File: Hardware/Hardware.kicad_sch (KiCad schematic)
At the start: 0 parts

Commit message: Finished SCH MCU
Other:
- added sheet IMU (IMU.kicad_sch)
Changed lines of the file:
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@@
 	(paper "A4")
 	(sheet
-		(at 166.37 92.71)
-		(size 73.66 48.26)
+		(at 59.69 35.56)
+		(size 36.83 19.05)
+		(fields_autoplaced yes)
+		(stroke
+			(width 0.1524)
+			(type solid)
+		)
+		(fill
+			(color 0 0 0 0.0000)
+		)
+		(property "Sheetname" "IMU"
+			(at 59.69 34.8484 0)
+			(effects
+				(font
+					(size 1.27 1.27)
+				)
+				(justify left bottom)
+			)
+		)
+		(property "Sheetfile" "IMU.kicad_sch"
+			(at 59.69 55.1946 0)
+			(effects
+				(font
+					(size 1.27 1.27)
+				)
+				(justify left top)
+			)
+		)
+		(instances
+			(project "Hardware"
+				(path "/8d39550c-1c23-48e1-ae23-c502e9088467"
+					(page "3")
+				)
+			)
+		)
+	)
+	(sheet
+		(at 15.24 17.78)
+		(size 21.59 48.26)
 		(fields_autoplaced yes)
 		(stroke
@@
 		)
 		(property "Sheetname" "MCU_Core"
-			(at 166.37 91.9984 0)
+			(at 15.24 17.0684 0)
 			(effects
 				(font
@@
 		)
 		(property "Sheetfile" "MCU_Core.kicad_sch"
-			(at 166.37 141.5546 0)
+			(at 15.24 66.6246 0)
 			(effects
 				(font

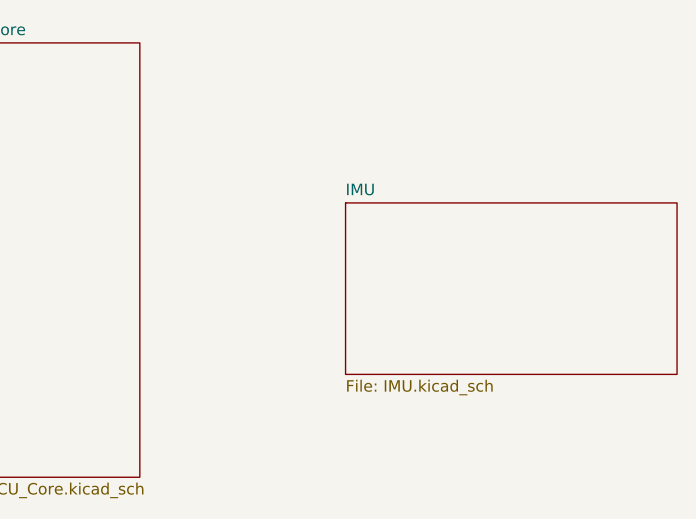
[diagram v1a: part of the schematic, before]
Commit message: Finished IMU SCH
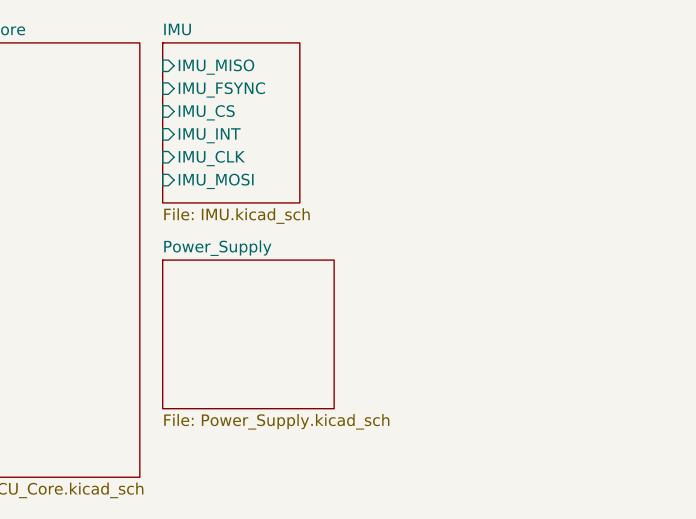
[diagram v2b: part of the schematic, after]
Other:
- added sheet Power_Supply (Power_Supply.kicad_sch)
- sheet IMU ports: added IMU_CLK, IMU_CS, IMU_FSYNC, IMU_INT, IMU_MISO, IMU_MOSI; removed none
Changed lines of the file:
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@@
 	(paper "A4")
 	(sheet
-		(at 59.69 35.56)
-		(size 36.83 19.05)
+		(at 39.37 17.78)
+		(size 15.24 17.78)
 		(fields_autoplaced yes)
 		(stroke
@@
 		)
 		(property "Sheetname" "IMU"
-			(at 59.69 34.8484 0)
+			(at 39.37 17.0684 0)
 			(effects
 				(font
@@
 		)
 		(property "Sheetfile" "IMU.kicad_sch"
-			(at 59.69 55.1946 0)
+			(at 39.37 36.1446 0)
 			(effects
 				(font
@@
 				)
 				(justify left top)
+			)
+		)
+		(pin "IMU_MISO" input
+			(at 39.37 20.32 180)
+			(effects
+				(font
+					(size 1.27 1.27)
+				)
+				(justify left)
+			)
+		)
+		(pin "IMU_FSYNC" input
+			(at 39.37 22.86 180)
+			(effects
+				(font
+					(size 1.27 1.27)
+				)
+				(justify left)
+			)
+		)
+		(pin "IMU_CS" input
+			(at 39.37 25.4 180)
+			(effects
+				(font
+					(size 1.27 1.27)
+				)
+				(justify left)
+			)
+		)
+		(pin "IMU_INT" input
+			(at 39.37 27.94 180)
+			(effects
+				(font
+					(size 1.27 1.27)
+				)
+				(justify left)
+			)
+		)
+		(pin "IMU_CLK" input
+			(at 39.37 30.48 180)
+			(effects
+				(font
+					(size 1.27 1.27)
+				)
+				(justify left)
+			)
+		)
+		(pin "IMU_MOSI" input
+			(at 39.37 33.02 180)
+			(effects
+				(font
+					(size 1.27 1.27)
+				)
+				(justify left)
 			)
 		)
@@
 				)
 			)
+		)
+	)
+	(sheet
+		(at 39.37 41.91)
+		(size 19.05 16.51)
+		(fields_autoplaced yes)
+		(stroke
+			(width 0.1524)
+			(type solid)
+		)
+		(fill
+			(color 0 0 0 0.0000)
+		)
+		(property "Sheetname" "Power_Supply"
+			(at 39.37 41.1984 0)
+			(effects
+				(font
+					(size 1.27 1.27)
+				)
+				(justify left bottom)
+			)
+		)
+		(property "Sheetfile" "Power_Supply.kicad_sch"
+			(at 39.37 59.0046 0)
+			(effects
+				(font
+					(size 1.27 1.27)
+				)
+				(justify left top)
+			)
+		)
+		(instances
+			(project "Hardware"
+				(path "/8d39550c-1c23-48e1-ae23-c502e9088467"
+					(page "4")
+				)
+			)
